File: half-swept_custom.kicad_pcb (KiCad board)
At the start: 2 copper layers, 108.6 x 86.9 mm, 22 parts, among them J2 AudioJack4dpb, SW10 SW_Push, SW11 SW_Push, SW12 SW_Push, SW14 SW_Push, SW15 SW_Push, SW16 SW_Push, SW17 SW_Push, SW18 SW_Push, SW2 SW_Push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

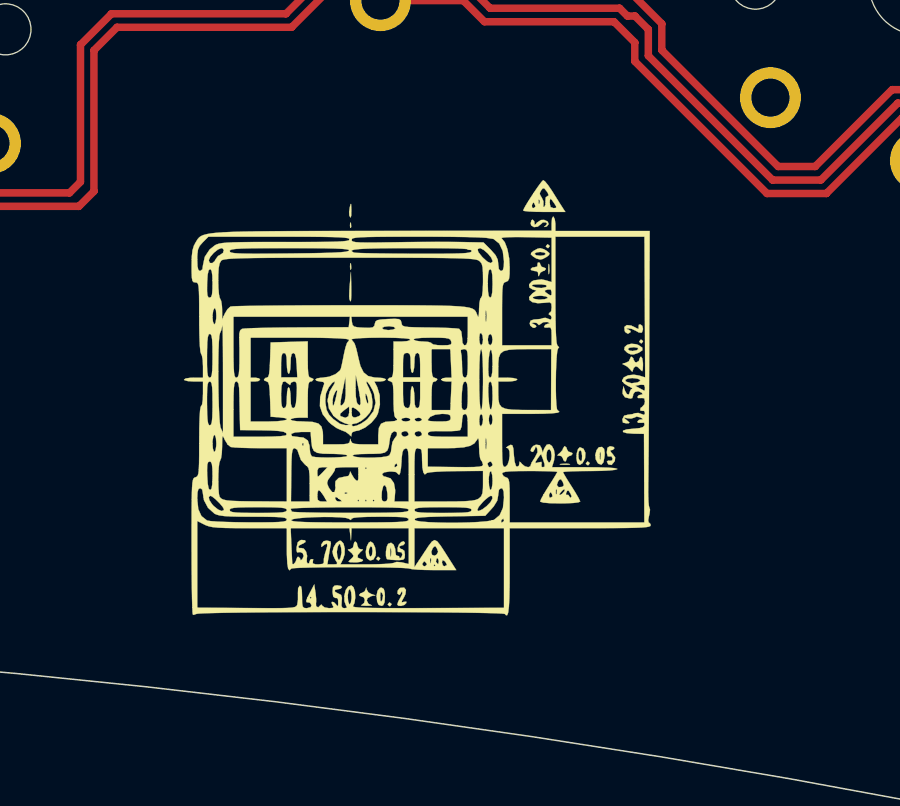
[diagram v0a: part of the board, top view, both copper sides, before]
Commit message: Align front and back switch silkscreen
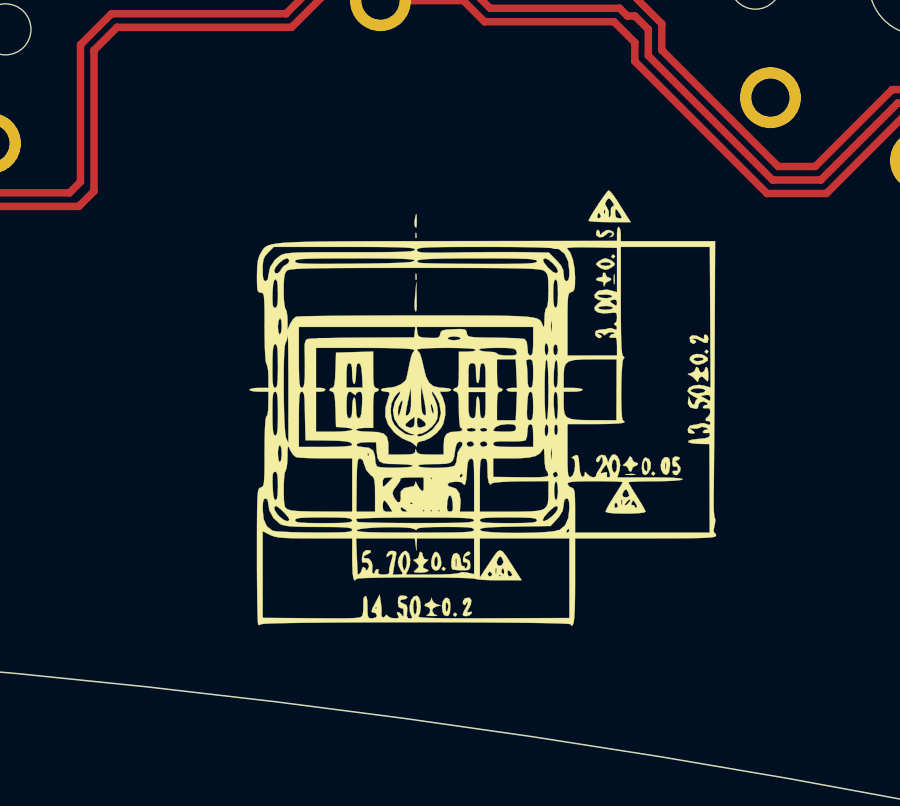
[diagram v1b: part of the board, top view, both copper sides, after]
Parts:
- moved REF** 2.21 mm to (59.2, 75.2)
- moved REF** 0.59 mm to (59.2, 75.1)
